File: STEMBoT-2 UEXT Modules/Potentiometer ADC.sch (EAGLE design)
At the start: 18 parts, among them IC1 74HC165PW,118, IC2 LMV324DR2G, IC3 LMV324DR2G, Q1 MMBT3904LP-7

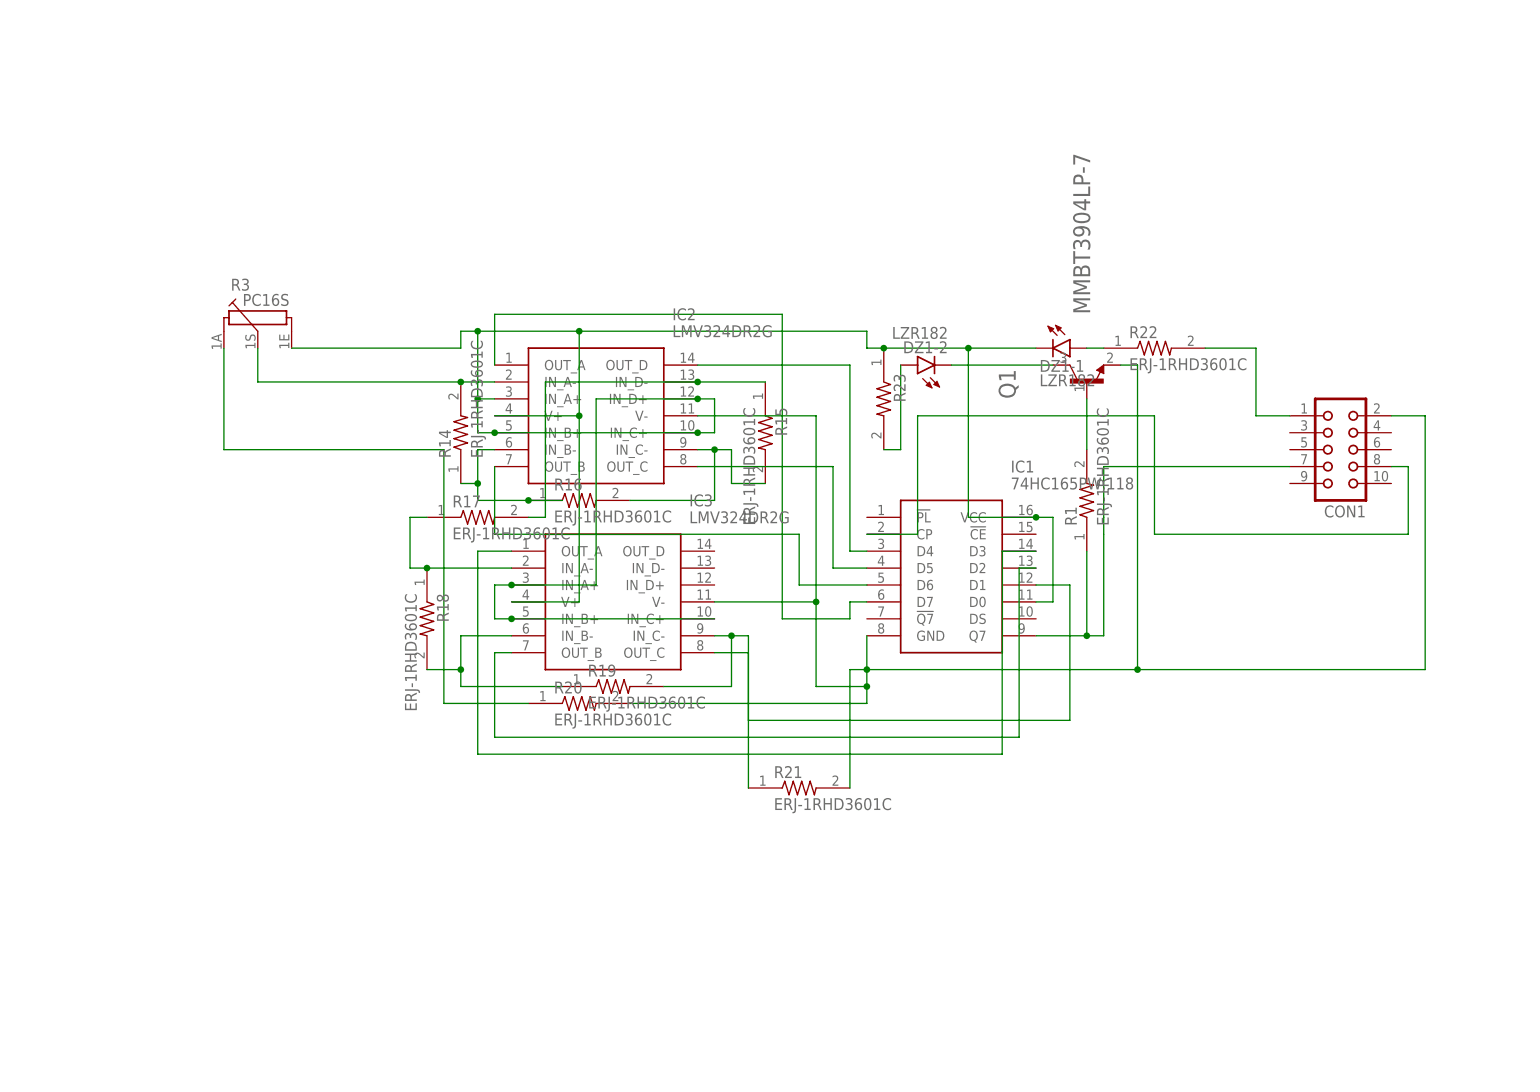
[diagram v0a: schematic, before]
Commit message: Adjusted ADC modules for PCB order. Dan, these are auto-routed.
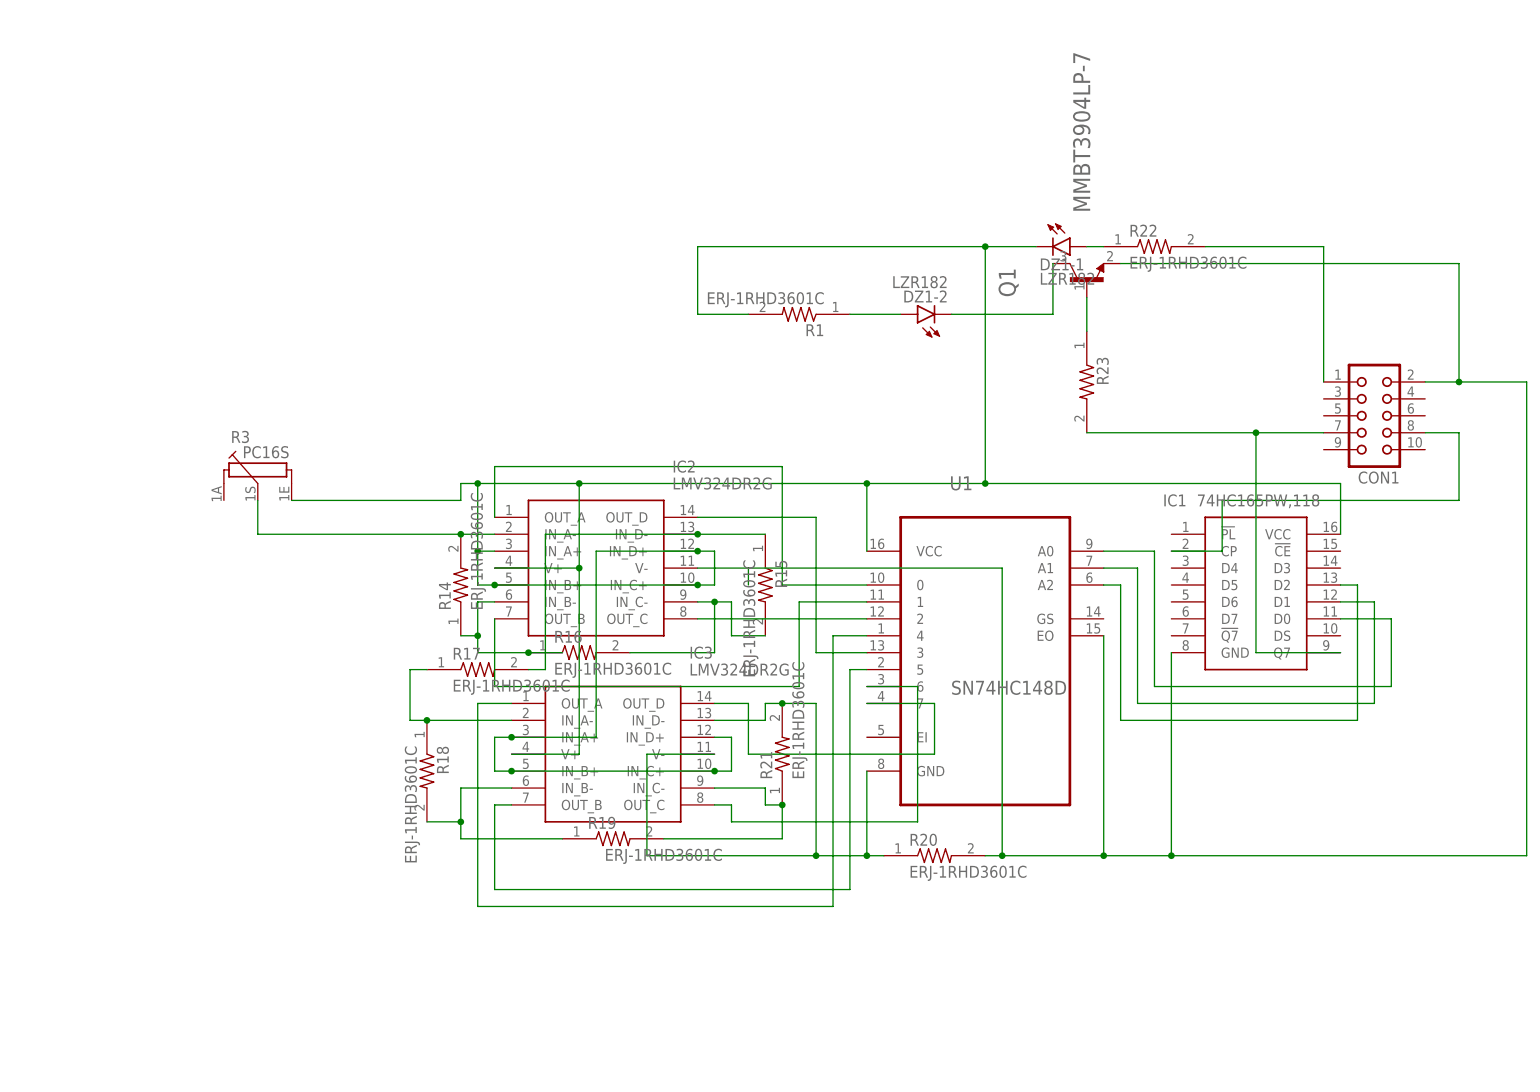
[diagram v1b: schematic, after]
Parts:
- added U1: SN74HC148D, SN74HC148D:SN74HC148D
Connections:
- removed net N$2 (its old number): CON1.2, IC1.GND, IC2.V-, IC3.V-, Q1.E, R20.2, R21.2
- removed net N$27: CON1.7, IC1.Q7, R1.1
- removed net N$30: IC1.D4, IC2.OUT_D
- new net N$12: CON1.2, IC1.GND, IC2.V-, Q1.E, R20.2, U1.EO
- new net N$16: IC1.D2, U1.A2
- new net N$19: CON1.7, IC1.Q7, R23.2
- new net N$20: Q1.B, R23.1
- new net N$22: DZ1-2.A, R1.1
- new net N$4: IC2.OUT_D, U1.3
- new net N$8: IC1.D0, U1.A0
- net N$1: now also IC3.IN_D-, IC3.V-, R20.1, R21.2, U1.GND; no longer Q1.B, R1.2
- net N$15: now also IC1.D1, U1.A1; no longer R20.1, R3.1A
- net N$23: now also U1.5; no longer IC1.D2
- net N$26: now also U1.4; no longer IC1.D3
- net N$31: now also U1.2; no longer IC1.D5
- net N$32: now also U1.1; no longer IC1.D6
- net N$33: now also U1.0; no longer IC1.D7
- net N$5: now also IC3.IN_D+, R1.2, U1.VCC; no longer IC1.D0, R23.1
- net N$6: now also U1.6; no longer IC1.D1
- net N$7: now also IC3.OUT_D, U1.7; no longer DZ1-2.A, R23.2
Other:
- moved on the sheet: CON1, DZ1-1, DZ1-2, IC1, IC2, IC3, Q1, R1, R14, R15, R16, R17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

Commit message: Once again, updating ADC shematics and boards. Used autorouter.
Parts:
- removed IC2, IC3: LMV324DR2G, LMV324DR2G:LMV324DR2G
- removed R20: ERJ-1RHD3601C, Resistor:ERJ-1RHD3601C
- added R2, R4: ERJ-1RHD3601C, Resistor:ERJ-1RHD3601C
- added U2, U3: MAX964ESET, MAX964ESET:MAX964ESET
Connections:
- removed net N$17: IC3.IN_C-, R19.2, R21.1
- removed net N$31: IC2.OUT_C, U1.2
- removed net N$32: IC2.OUT_B, U1.1
- removed net N$33: IC2.OUT_A, U1.0
- removed net N$5: DZ1-1.C, IC1.VCC, IC2.IN_A+, IC2.IN_B+, IC2.IN_C+, IC2.IN_D+, IC2.V+, IC3.IN_A+, IC3.IN_B+, IC3.IN_C+, IC3.IN_D+, IC3.V+, R1.2, R3.1E, U1.VCC
- new net N$21: U1.5, U2.QC
- new net N$27: U1.2, U3.QB
- new net N$28: U1.1, U3.QC
- new net N$29: U1.0, U3.QD
- new net N$30: DZ1-1.C, IC1.VCC, R1.2, R3.1E, R3.1S, R4.2, U1.VCC, U2.INA+, U2.INB+, U2.INC+, U2.IND+, U2.VCC, U3.INA+, U3.INB+, U3.INC+, U3.IND+, U3.VCC
- net N$1: now also R16.1, R2.2, U3.INC-; no longer IC3.IN_D-, IC3.V-, R20.1, R21.2, U1.GND
- net N$10: now also R16.2, R21.1, U3.INB-; no longer IC2.IN_B-, R14.1, R16.1
- net N$11: now also R19.1, R2.1, U3.IND-; no longer IC2.IN_A-, R14.2, R3.1S
- net N$12: now also R19.2, U1.GND, U2.GND, U3.GND; no longer IC2.V-, R20.2
- net N$13: now also U1.7, U2.QA; no longer IC2.IN_C-, R15.2, R16.2
- net N$14: now also U1.6, U2.QB; no longer IC2.IN_D-, R15.1, R17.2
- net N$23: now also U1.3, U2.QD; no longer IC3.OUT_B, U1.5
- net N$26: now also U3.QA; no longer IC3.OUT_A
- net N$3: now also R14.2, R4.1, U2.INA-; no longer IC3.IN_A-, R17.1, R18.1
- net N$4: now also R14.1, R15.1, U2.INB-; no longer IC2.OUT_D, U1.3
- net N$6: now also R15.2, R18.1, U2.INC-; no longer IC3.OUT_C, U1.6
- net N$7: now also R17.2, R18.2, U2.IND-; no longer IC3.OUT_D, U1.7
- net N$9: now also R17.1, R21.2, U3.INA-; no longer IC3.IN_B-, R18.2, R19.1
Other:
- moved on the sheet: R14, R15, R16, R17, R18, R19, R21, R3, U1
